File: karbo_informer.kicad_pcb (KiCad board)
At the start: 2 copper layers, 12 parts, among them IC1 MAX7219, IC2 MAX7219, P1 USB_OTG

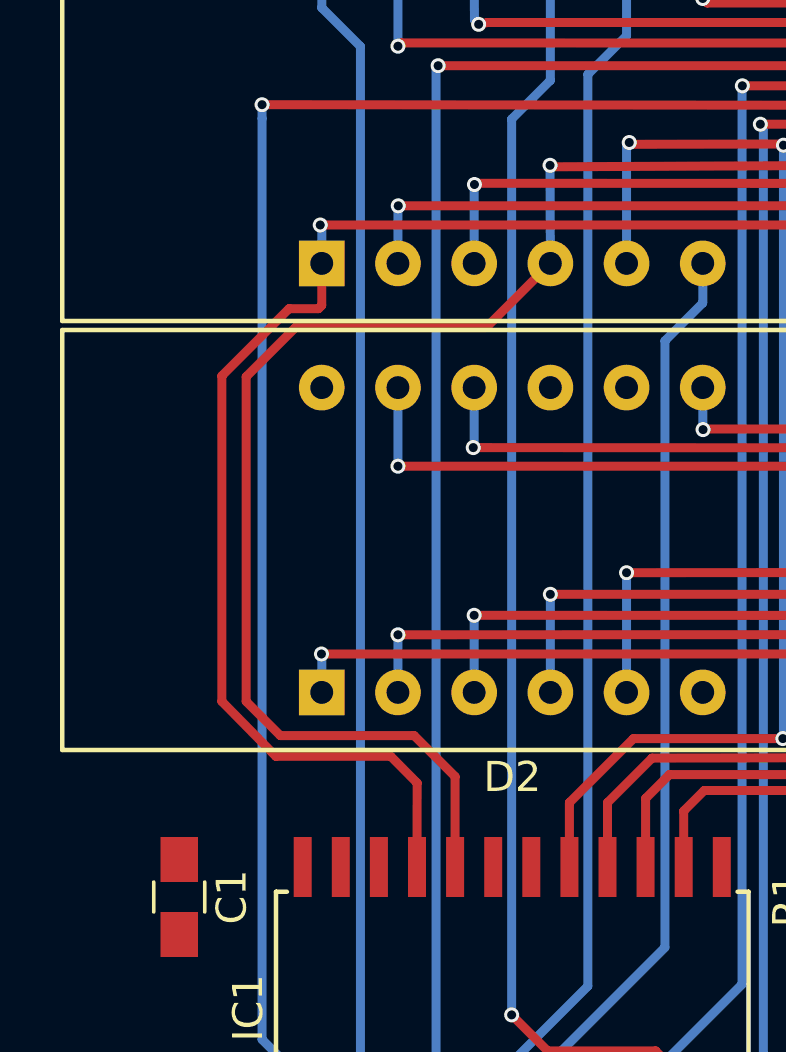
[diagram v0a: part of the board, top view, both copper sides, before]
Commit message: Wire for SEG_DP to MAX7219 in the buy line
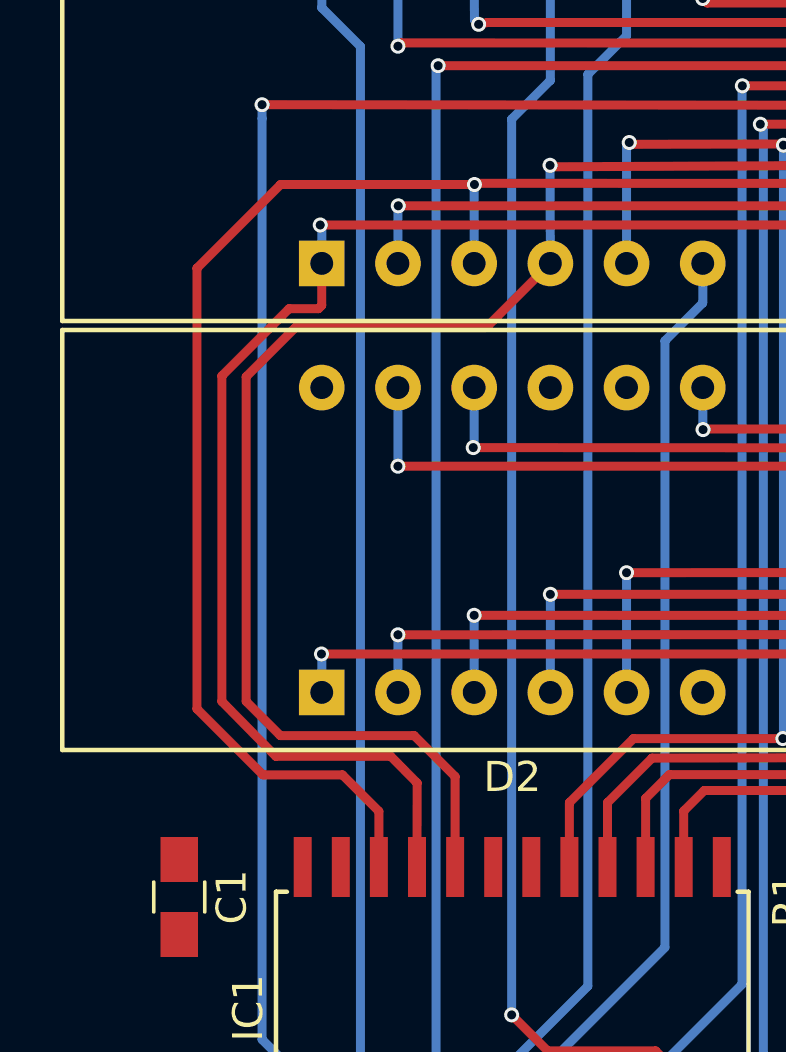
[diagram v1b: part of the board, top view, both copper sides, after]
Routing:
- net /B_SEG_DP: track 35.6 -> 70.0 mm
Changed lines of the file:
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@@
   (general
     (links 69)
-    (no_connects 39)
+    (no_connects 38)
     (area 0 0 0 0)
     (thickness 1.6)
     (drawings 0)
-    (tracks 243)
+    (tracks 252)
     (zones 0)
     (modules 12)
@@
   (segment (start 34.4 32.7) (end 34.4 32.7) (width 0.3) (layer F.Cu) (net 1))
   (via (at 34.4 32.7) (size 0.5) (drill 0.3) (layers F.Cu B.Cu) (net 1))
+  (segment (start 32.5 51.02) (end 32.48 51.02) (width 0.3) (layer F.Cu) (net 2))
+  (segment (start 36.355 52.245) (end 35.14 51.03) (width 0.3) (layer F.Cu) (net 2))
+  (segment (start 35.14 51.03) (end 32.51 51.03) (width 0.3) (layer F.Cu) (net 2))
+  (segment (start 32.51 51.03) (end 32.5 51.02) (width 0.3) (layer F.Cu) (net 2))
+  (segment (start 36.355 54.1) (end 36.355 52.245) (width 0.3) (layer F.Cu) (net 2) (status 400000))
+  (segment (start 33.08 31.35) (end 39.54 31.35) (width 0.3) (layer F.Cu) (net 2))
+  (segment (start 30.29 34.14) (end 33.08 31.35) (width 0.3) (layer F.Cu) (net 2))
+  (segment (start 30.29 48.83) (end 30.29 34.14) (width 0.3) (layer F.Cu) (net 2))
+  (segment (start 32.48 51.02) (end 30.29 48.83) (width 0.3) (layer F.Cu) (net 2))
   (segment (start 39.53 33.98) (end 39.53 31.36) (width 0.3) (layer B.Cu) (net 2))
   (segment (start 69.81 31.33) (end 69.83 33.98) (width 0.3) (layer B.Cu) (net 2))

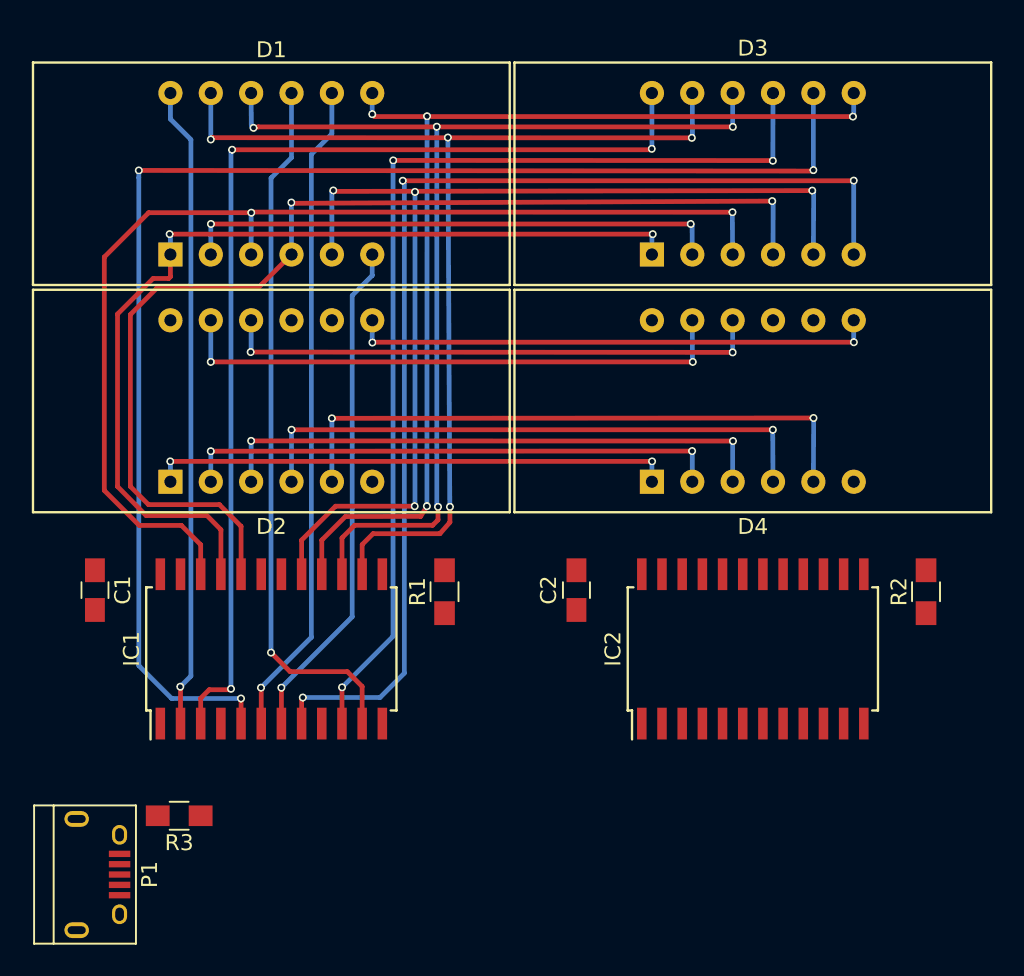
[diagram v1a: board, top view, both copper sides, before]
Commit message: Wire for SEG_D to MAX7219 in the buy line
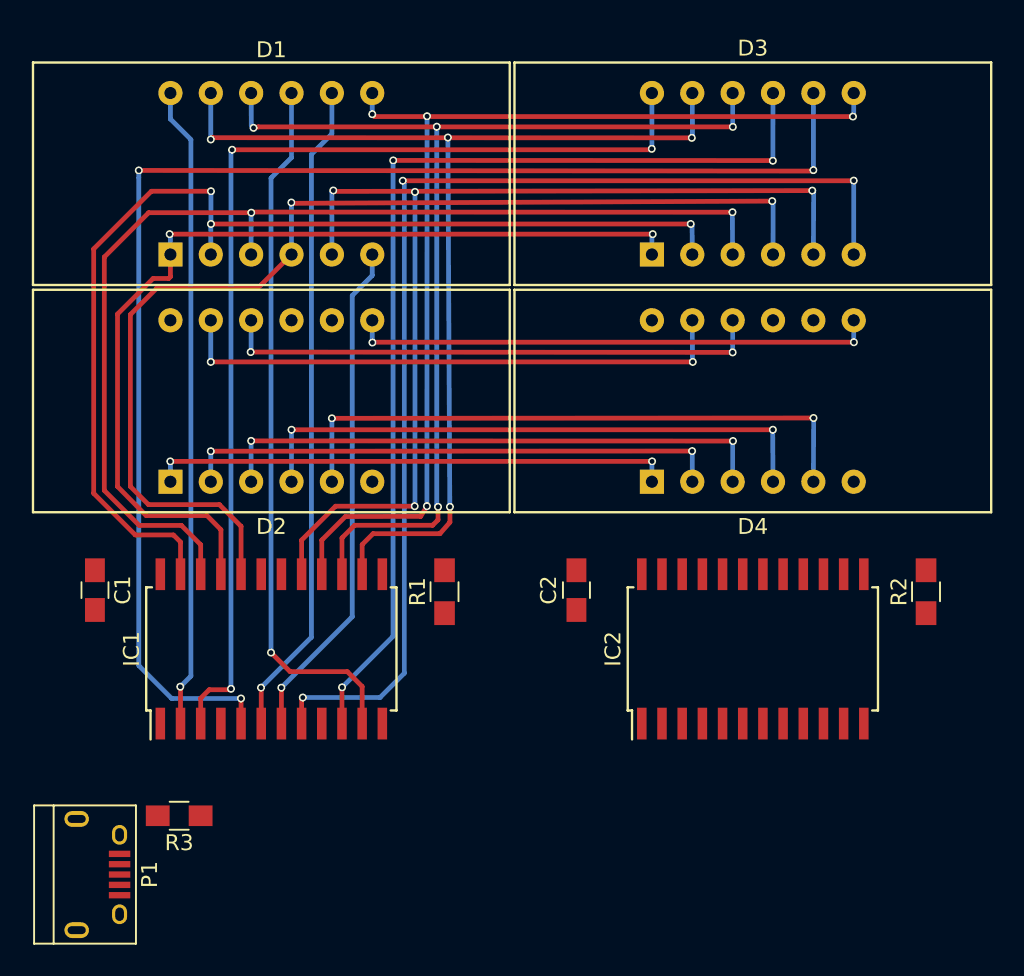
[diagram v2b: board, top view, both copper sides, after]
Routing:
- net /B_SEG_D: track 34.1 -> 69.1 mm, vias 2 -> 3
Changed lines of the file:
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@@
   (general
     (links 69)
-    (no_connects 38)
+    (no_connects 37)
     (area 0 0 0 0)
     (thickness 1.6)
     (drawings 0)
-    (tracks 252)
+    (tracks 261)
     (zones 0)
     (modules 12)
@@
   (via (at 39.54 31.35) (size 0.5) (drill 0.3) (layers F.Cu B.Cu) (net 2))
   (segment (start 39.53 31.36) (end 39.54 31.35) (width 0.3) (layer B.Cu) (net 2))
+  (via (at 37 30) (size 0.5) (drill 0.3) (layers F.Cu B.Cu) (net 3))
+  (via (at 37 32.06) (size 0.5) (drill 0.3) (layers F.Cu B.Cu) (net 3))
+  (segment (start 37 32.06) (end 67.19 32.06) (width 0.3) (layer F.Cu) (net 3))
+  (via (at 67.19 32.06) (size 0.5) (drill 0.3) (layers F.Cu B.Cu) (net 3))
+  (segment (start 67.19 32.06) (end 67.28 32.15) (width 0.3) (layer B.Cu) (net 3))
+  (segment (start 67.29 33.98) (end 67.28 32.15) (width 0.3) (layer B.Cu) (net 3))
+  (segment (start 35.085 52.075) (end 34.64 51.63) (width 0.3) (layer F.Cu) (net 3))
+  (segment (start 34.64 51.63) (end 32.24 51.63) (width 0.3) (layer F.Cu) (net 3))
+  (segment (start 32.24 51.63) (end 29.62 49.01) (width 0.3) (layer F.Cu) (net 3))
+  (segment (start 29.62 49.01) (end 29.62 33.63) (width 0.3) (layer F.Cu) (net 3))
+  (segment (start 29.62 33.63) (end 33.25 30) (width 0.3) (layer F.Cu) (net 3))
+  (segment (start 33.25 30) (end 37 30) (width 0.3) (layer F.Cu) (net 3))
+  (segment (start 35.085 52.075) (end 35.085 54.1) (width 0.3) (layer F.Cu) (net 3) (status 800000))
+  (segment (start 37 30) (end 37 32.06) (width 0.3) (layer B.Cu) (net 3))
   (segment (start 36.99 33.98) (end 36.99 32.07) (width 0.3) (layer B.Cu) (net 3))
-  (segment (start 67.28 32.15) (end 67.29 33.98) (width 0.3) (layer B.Cu) (net 3))
-  (segment (start 67.19 32.06) (end 67.28 32.15) (width 0.3) (layer B.Cu) (net 3))
-  (via (at 67.19 32.06) (size 0.5) (drill 0.3) (layers F.Cu B.Cu) (net 3))
-  (segment (start 37 32.06) (end 67.19 32.06) (width 0.3) (layer F.Cu) (net 3))
-  (via (at 37 32.06) (size 0.5) (drill 0.3) (layers F.Cu B.Cu) (net 3))
   (segment (start 38.895 54.1) (end 38.895 51.085) (width 0.3) (layer F.Cu) (net 4) (status 400000))
   (segment (start 39.93 36.12) (end 42.07 33.98) (width 0.3) (layer F.Cu) (net 4) (status 800000))

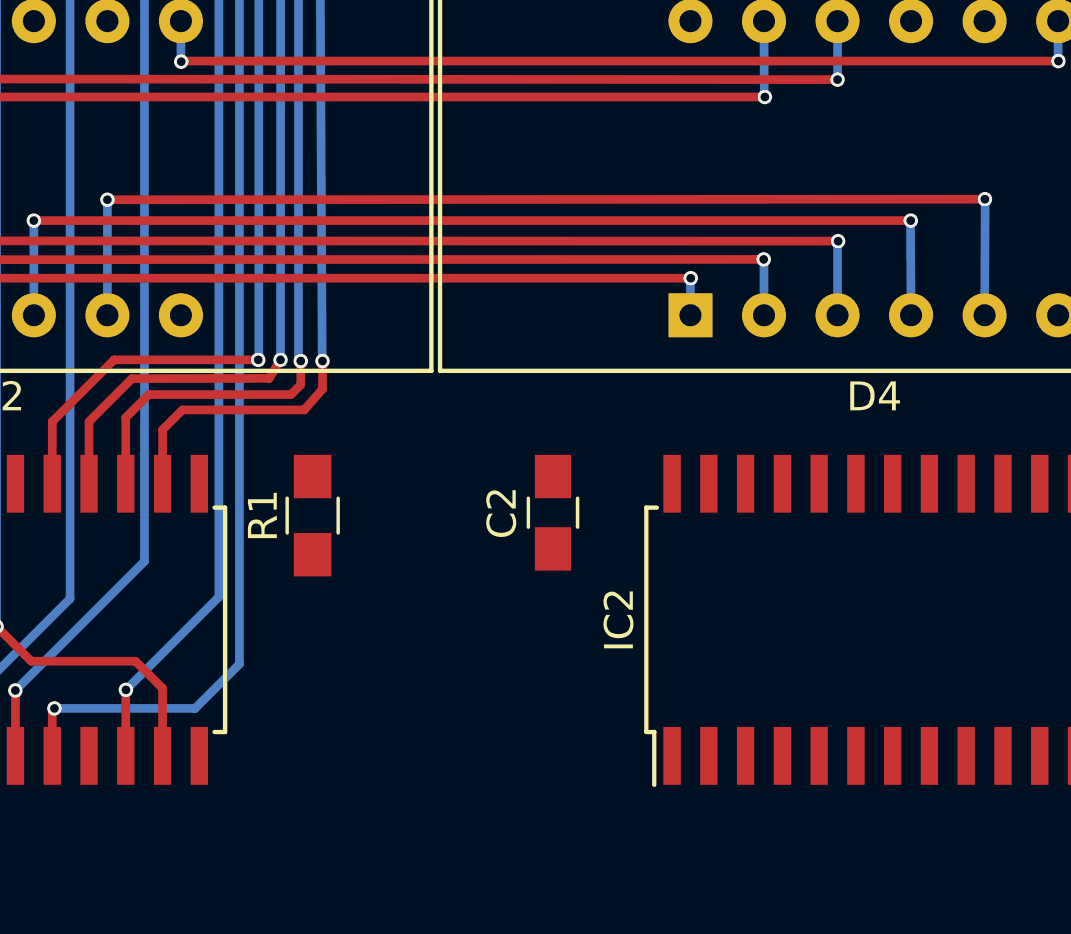
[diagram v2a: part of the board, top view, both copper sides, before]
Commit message: Wire for DIG_3 to MAX7219 in the sell line
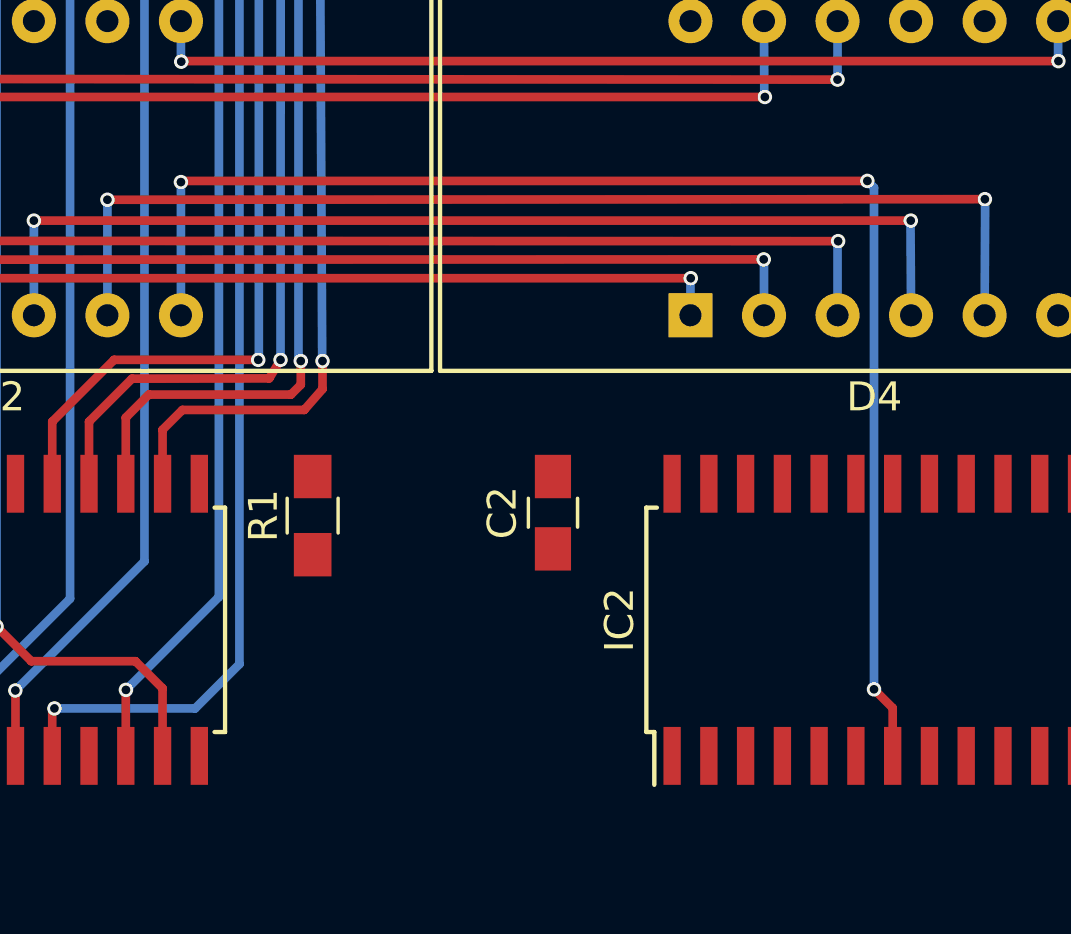
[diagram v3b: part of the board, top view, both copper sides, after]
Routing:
- net /S_DIG_3: track 0.00 -> 48.5 mm, vias 0 -> 3
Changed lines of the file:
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@@
   (general
     (links 69)
-    (no_connects 37)
-    (area 0 0 0 0)
+    (no_connects 36)
+    (area 23.915 20.025 86.425001 77.825001)
     (thickness 1.6)
     (drawings 0)
-    (tracks 261)
+    (tracks 271)
     (zones 0)
     (modules 12)
@@
     )
   )
-  (segment (start 37.625 54.1) (end 37.63 51.3) (width 0.3) (layer F.Cu) (net 1) (status 400000))
-  (segment (start 34.45 35.38) (end 34.45 33.98) (width 0.3) (layer F.Cu) (net 1) (status 800000))
+  (segment (start 37.625 54.1) (end 37.63 51.3) (width 0.3) (layer F.Cu) (net 1))
+  (segment (start 34.45 35.38) (end 34.45 33.98) (width 0.3) (layer F.Cu) (net 1))
   (segment (start 34.34 35.49) (end 34.45 35.38) (width 0.3) (layer F.Cu) (net 1))
   (segment (start 33.36 35.49) (end 34.34 35.49) (width 0.3) (layer F.Cu) (net 1))
@@
   (segment (start 35.14 51.03) (end 32.51 51.03) (width 0.3) (layer F.Cu) (net 2))
   (segment (start 32.51 51.03) (end 32.5 51.02) (width 0.3) (layer F.Cu) (net 2))
-  (segment (start 36.355 54.1) (end 36.355 52.245) (width 0.3) (layer F.Cu) (net 2) (status 400000))
+  (segment (start 36.355 54.1) (end 36.355 52.245) (width 0.3) (layer F.Cu) (net 2))
   (segment (start 33.08 31.35) (end 39.54 31.35) (width 0.3) (layer F.Cu) (net 2))
   (segment (start 30.29 34.14) (end 33.08 31.35) (width 0.3) (layer F.Cu) (net 2))
@@
   (segment (start 29.62 33.63) (end 33.25 30) (width 0.3) (layer F.Cu) (net 3))
   (segment (start 33.25 30) (end 37 30) (width 0.3) (layer F.Cu) (net 3))
-  (segment (start 35.085 52.075) (end 35.085 54.1) (width 0.3) (layer F.Cu) (net 3) (status 800000))
+  (segment (start 35.085 52.075) (end 35.085 54.1) (width 0.3) (layer F.Cu) (net 3))
   (segment (start 37 30) (end 37 32.06) (width 0.3) (layer B.Cu) (net 3))
   (segment (start 36.99 33.98) (end 36.99 32.07) (width 0.3) (layer B.Cu) (net 3))
-  (segment (start 38.895 54.1) (end 38.895 51.085) (width 0.3) (layer F.Cu) (net 4) (status 400000))
-  (segment (start 39.93 36.12) (end 42.07 33.98) (width 0.3) (layer F.Cu) (net 4) (status 800000))
+  (segment (start 38.895 54.1) (end 38.895 51.085) (width 0.3) (layer F.Cu) (net 4))
+  (segment (start 39.93 36.12) (end 42.07 33.98) (width 0.3) (layer F.Cu) (net 4))
   (segment (start 33.57 36.12) (end 39.93 36.12) (width 0.3) (layer F.Cu) (net 4))
   (segment (start 31.93 37.76) (end 33.57 36.12) (width 0.3) (layer F.Cu) (net 4))
@@
   (segment (start 45.89 36.56) (end 45.89 56.78) (width 0.3) (layer B.Cu) (net 6))
   (segment (start 47.15 35.3) (end 45.89 36.56) (width 0.3) (layer B.Cu) (net 6))
-  (segment (start 45.245 54.1) (end 45.245 51.815) (width 0.3) (layer F.Cu) (net 7) (status 400000))
+  (segment (start 45.245 54.1) (end 45.245 51.815) (width 0.3) (layer F.Cu) (net 7))
   (via (at 51.21 25.94) (size 0.5) (drill 0.3) (layers F.Cu B.Cu) (net 7))
   (segment (start 51.21 49.78) (end 51.21 25.94) (width 0.3) (layer B.Cu) (net 7))
@@
   (segment (start 47.2 51.55) (end 51.41 51.55) (width 0.3) (layer F.Cu) (net 8))
   (segment (start 51.41 51.55) (end 52.04 50.83) (width 0.3) (layer F.Cu) (net 8))
-  (segment (start 46.515 54.1) (end 46.515 52.235) (width 0.3) (layer F.Cu) (net 8) (status 400000))
+  (segment (start 46.515 54.1) (end 46.515 52.235) (width 0.3) (layer F.Cu) (net 8))
   (via (at 52.04 49.86) (size 0.5) (drill 0.3) (layers F.Cu B.Cu) (net 8))
   (segment (start 51.909995 26.620005) (end 51.909995 26.63491) (width 0.3) (layer F.Cu) (net 8))
@@
   (segment (start 44.62 44.29) (end 74.92 44.27) (width 0.3) (layer F.Cu) (net 17))
   (via (at 44.61 44.29) (size 0.5) (drill 0.3) (layers F.Cu B.Cu) (net 17))
+  (segment (start 70.86 43.64) (end 71.09 43.87) (width 0.3) (layer B.Cu) (net 18))
+  (via (at 70.86 43.64) (size 0.5) (drill 0.3) (layers F.Cu B.Cu) (net 18))
+  (via (at 47.15 43.68) (size 0.5) (drill 0.3) (layers F.Cu B.Cu) (net 18))
+  (segment (start 47.15 43.68) (end 47.19 43.64) (width 0.3) (layer F.Cu) (net 18))
+  (segment (start 47.19 43.64) (end 70.86 43.64) (width 0.3) (layer F.Cu) (net 18))
+  (segment (start 71.09 43.87) (end 71.09 61.2) (width 0.3) (layer B.Cu) (net 18))
+  (via (at 71.09 61.2) (size 0.5) (drill 0.3) (layers F.Cu B.Cu) (net 18))
+  (segment (start 71.09 61.2) (end 71.735 61.845) (width 0.3) (layer F.Cu) (net 18))
+  (segment (start 71.735 63.5) (end 71.735 61.845) (width 0.3) (layer F.Cu) (net 18))
+  (segment (start 47.15 43.68) (end 47.15 48.28) (width 0.3) (layer B.Cu) (net 18))
   (via (at 39.5 40.12) (size 0.5) (drill 0.3) (layers F.Cu B.Cu) (net 19))
   (segment (start 39.5 40.12) (end 69.83 40.14) (width 0.3) (layer F.Cu) (net 19))
